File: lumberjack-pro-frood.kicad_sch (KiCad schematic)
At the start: 159 parts, among them J1 USB, J2 AVR_ISP_6, J3 JST, J4 JST, SW1 RESET, SW2 BOOT, U1 ATMEGA328-PU, Y1 16MHz

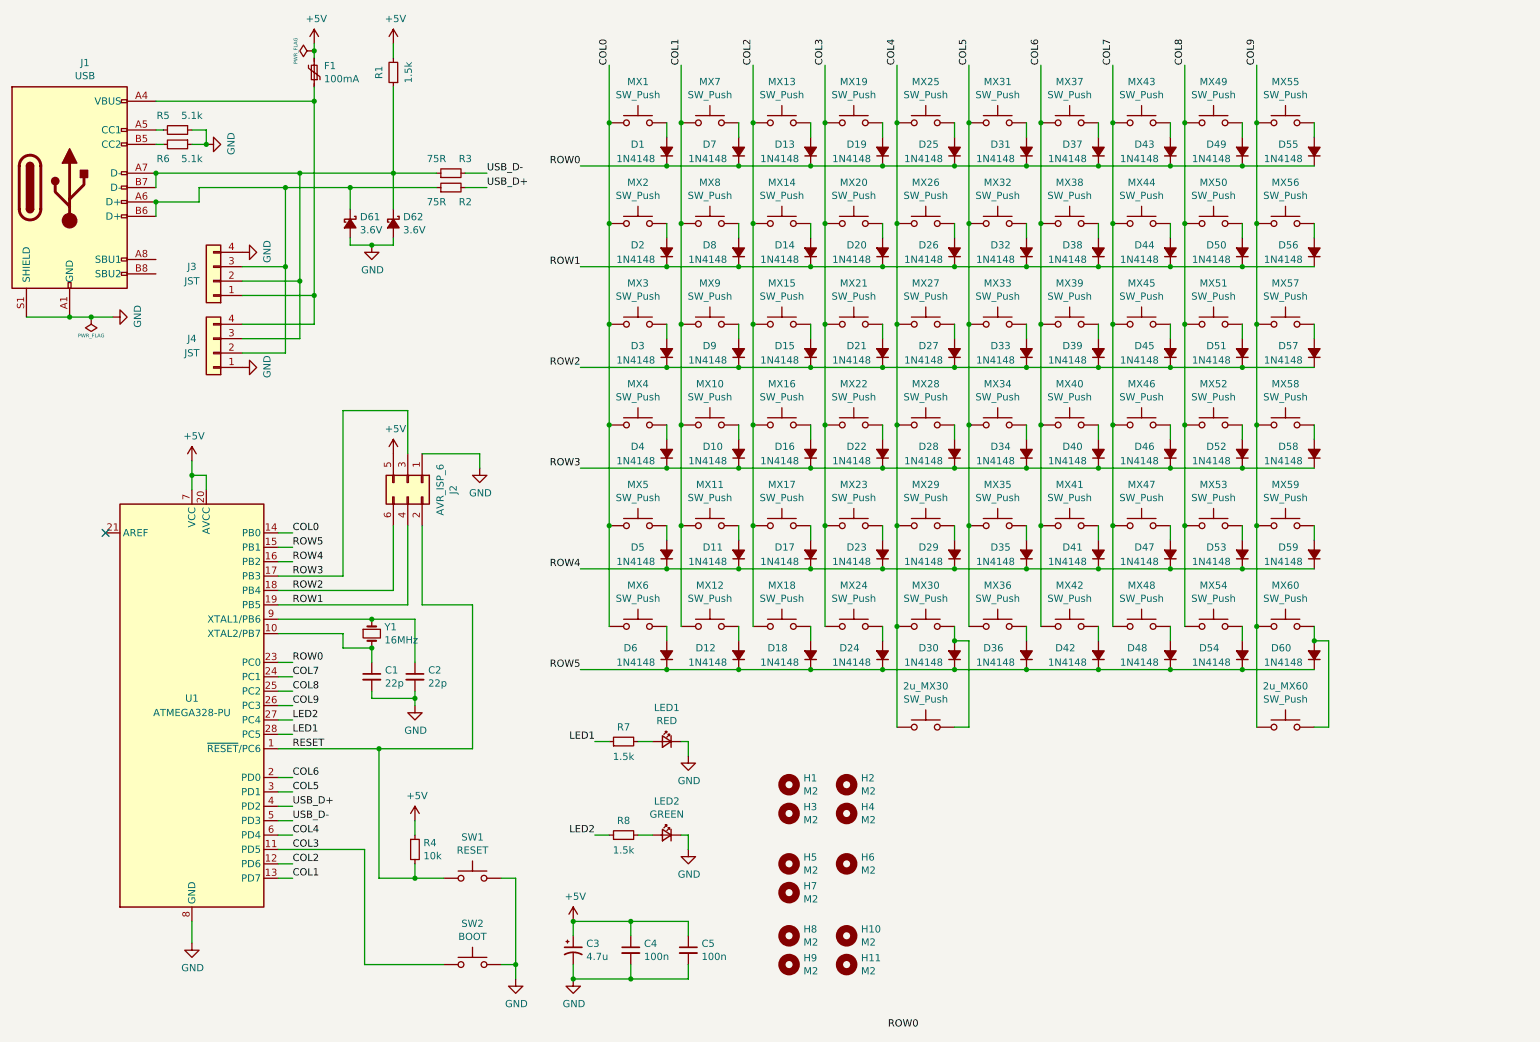
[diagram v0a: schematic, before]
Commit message: WIP: replace discrete MCU with the Frood
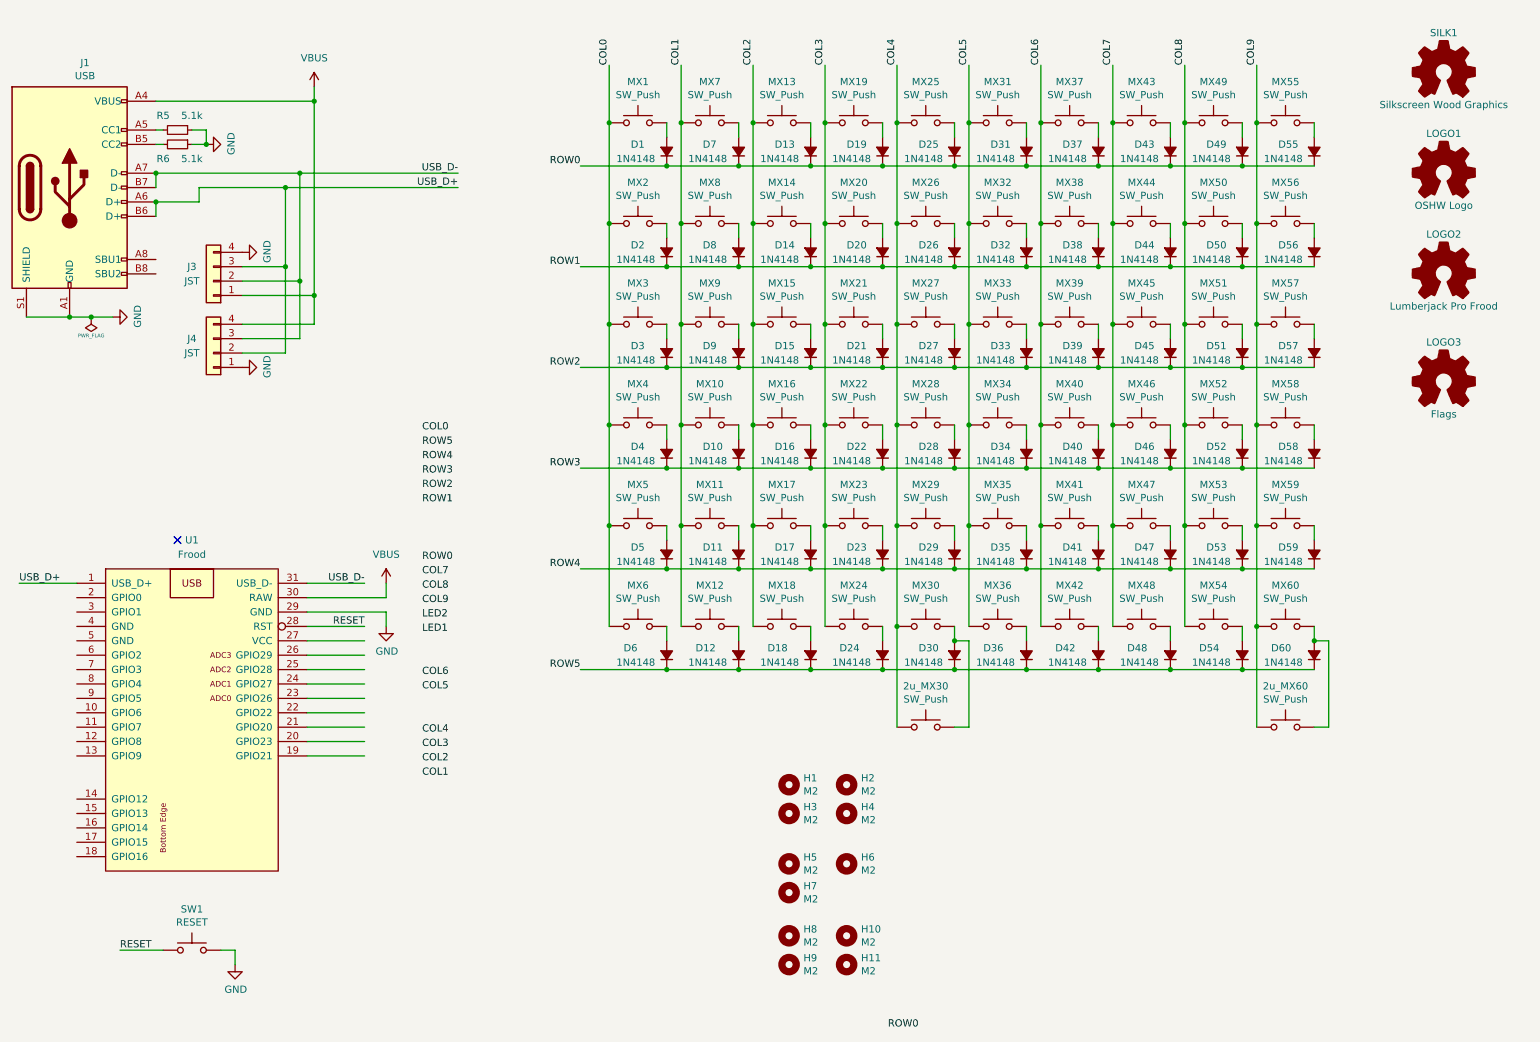
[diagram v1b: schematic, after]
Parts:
- removed C1, C2: 22p, Capacitor_THT:C_Disc_D3.0mm_W1.6mm_P2.50mm, symbol Device:C_Small
- removed C3: 4.7u, Capacitor_THT:CP_Radial_D4.0mm_P1.50mm, symbol lumberjack-rescue:CP1_Small-Device
- removed C4, C5: 100n, Capacitor_THT:C_Disc_D4.3mm_W1.9mm_P5.00mm, symbol Device:C_Small
- removed D61, D62: 3.6V, Diode_THT:D_DO-35_SOD27_P7.62mm_Horizontal, symbol lumberjack-rescue:D_Schottky_Small_ALT-Device
- removed F1: 100mA, Fuse:Fuse_Bourns_MF-RHT100, symbol Device:Polyfuse_Small
- removed J2: AVR_ISP_6, Connector_PinHeader_2.54mm:PinHeader_2x03_P2.54mm_Vertical, symbol Connector_Generic:Conn_02x03_Odd_Even
- removed LED1: RED, LED_THT:LED_D3.0mm, symbol Device:LED_Small
- removed LED2: GREEN, LED_THT:LED_D3.0mm, symbol Device:LED_Small
- removed R1, R7, R8: 1.5k, Resistor_THT:R_Axial_DIN0204_L3.6mm_D1.6mm_P7.62mm_Horizontal, symbol Device:R_Small
- removed R2, R3: 75R, Resistor_THT:R_Axial_DIN0204_L3.6mm_D1.6mm_P7.62mm_Horizontal, symbol Device:R_Small
- removed R4: 10k, Resistor_THT:R_Axial_DIN0204_L3.6mm_D1.6mm_P7.62mm_Horizontal, symbol Device:R_Small
- removed SW2: BOOT, Button_Switch_THT:SW_PUSH_6mm, symbol Switch:SW_Push
- removed U1: ATMEGA328-PU, Package_DIP:DIP-28_W7.62mm, symbol lumberjack-rescue:ATmega328P-PU-MCU_Microchip_ATmega
- removed Y1: 16MHz, Crystal:Crystal_HC49-4H_Vertical, symbol Device:Crystal_Small
- added LOGO1: OSHW Logo, lumberjack:OSHW, symbol Graphic:Logo_Open_Hardware_Small
- added LOGO2: Lumberjack Pro Frood, lumberjack:Lumberjack-Pro-Frood, symbol Graphic:Logo_Open_Hardware_Small
- added LOGO3: Flags, lumberjack:Flags-NL-CZ-EU, symbol Graphic:Logo_Open_Hardware_Small
- added SILK1: Silkscreen Wood Graphics, lumberjack:wood, symbol Graphic:Logo_Open_Hardware_Small
- added U1: Frood, 42keebs:Frood_PinHeader_2x13+5_P2.54mm_Labels_Top, symbol 42keebs:Frood
- SW1: footprint Button_Switch_THT:SW_PUSH_6mm -> 42keebs:TACT_SWITCH_TVBP06
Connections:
- net GND: now also U1.29 (GND)
- net RESET: now also U1.28 (RST)
- net USB_D+: now also J1.A6 (D+), J1.B6 (D+), J3.3 (Pin_3), J4.2 (Pin_2), U1.1 (USB_D+)
- net USB_D-: now also J1.A7 (D-), J1.B7 (D-), J3.2 (Pin_2), J4.3 (Pin_3), U1.31 (USB_D-)
- net VBUS: now reaches J1.A4 (VBUS), J1.A9 (VBUS), J1.B4 (VBUS), J1.B9 (VBUS), J3.1 (Pin_1), J4.4 (Pin_4)
- net VBUS: now also U1.30 (RAW)
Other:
- moved on the sheet: SW1
